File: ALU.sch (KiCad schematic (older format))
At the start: 0 parts

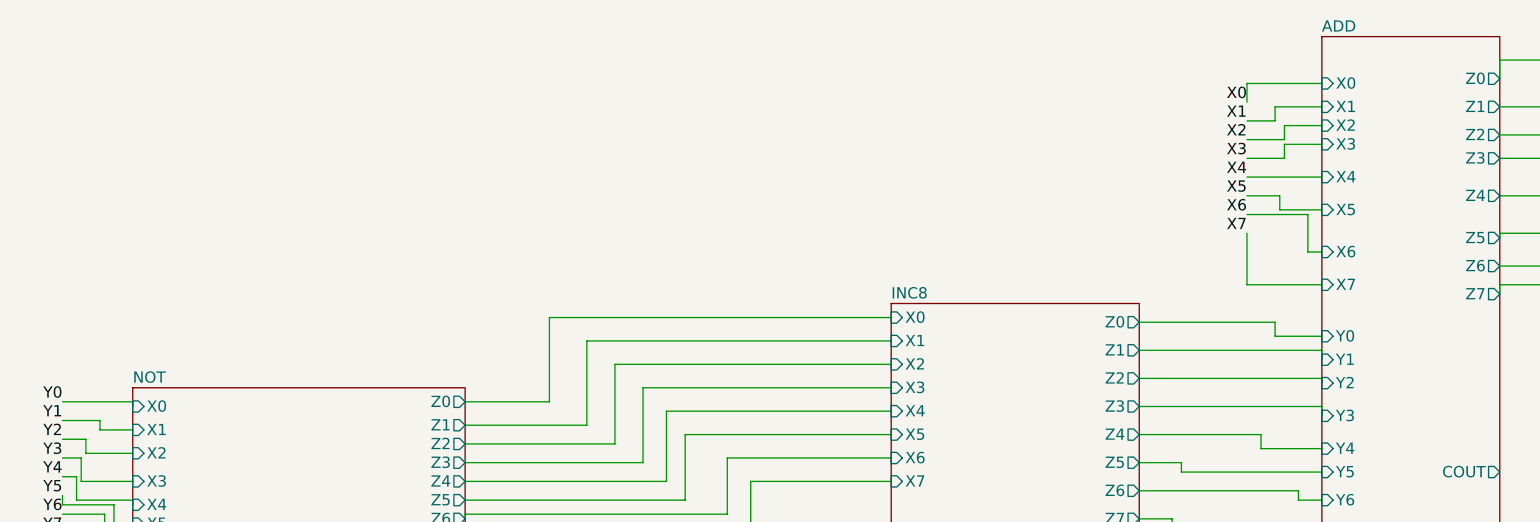
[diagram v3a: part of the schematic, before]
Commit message: fixed duplicate names
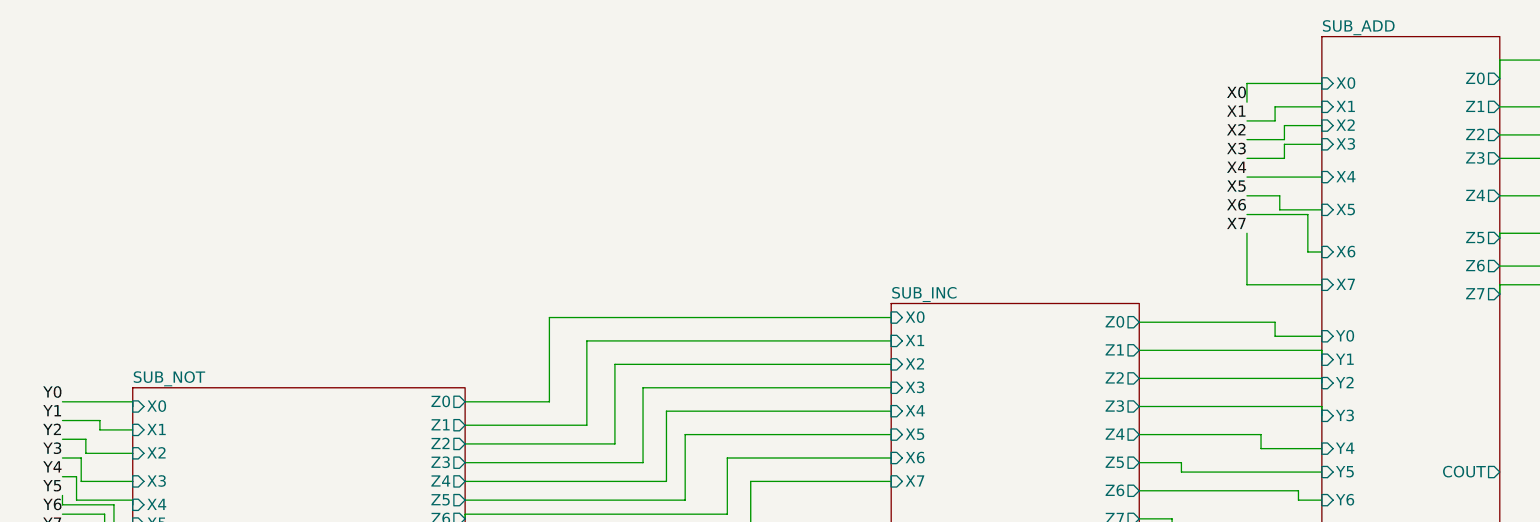
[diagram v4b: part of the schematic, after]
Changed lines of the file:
@@
 S 5625 7375 1775 1150
 U 5AE6649D
-F0 "NOT" 60
+F0 "SUB_NOT" 60
 F1 "NOT.sch" 60
 F2 "X0" I L 5625 7475 60
@@
 S 9675 6925 1325 1625
 U 5AE74AF7
-F0 "INC8" 60
+F0 "SUB_INC" 60
 F1 "INC8.sch" 60
 F2 "X0" I L 9675 7000 60
@@
 S 11975 5500 950  3075
 U 5AE93FA0
-F0 "ADD" 60
+F0 "SUB_ADD" 60
 F1 "ADD.sch" 60
 F2 "X0" I L 11975 5750 60

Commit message: NC-symbols
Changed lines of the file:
@@
 F16 "Z6" O R 8100 20300 60
 F17 "Z7" O R 8100 20450 60
+F18 "C_OUT" O R 8100 20525 60
 $EndSheet
 $Sheet

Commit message: lots of work done
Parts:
- added C1: 100nF, symbol spice:C
- added U1: 74LS08, symbol 74xx:74LS08
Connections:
- net labels added: 0, Cin, CinE, Cout, Cout_0, Cout_4, Cout_5, Cout_6, S0, S1, S2, S3, VCC, Z0, Z1, Z2, Z3, Z4, Z5, Z6, Z7
- wire segments 818 -> 929
- no-connect marks 0 -> 13

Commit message: X
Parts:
- added C? (x2): 100nF, symbol pspice:C
- added U? (x8): 74LS32, symbol 74xx:74LS32
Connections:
- net labels added: GND, ZFlag
- wire segments 929 -> 965
- no-connect marks 13 -> 14
